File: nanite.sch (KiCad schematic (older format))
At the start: 13 parts

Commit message: Add values
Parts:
- C?: value C -> 100n
- D? (x2): value D_Zener -> 3.6V
- R?: value R -> 390
- R? (x2): value R -> 68
- R?: value R -> 1k5
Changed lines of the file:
@@
 P 3350 3100
 F 0 "D?" H 3350 3200 50  0000 C CNN
-F 1 "D_Zener" H 3350 3000 50  0000 C CNN
+F 1 "3.6V" H 3350 3000 50  0000 C CNN
 F 2 "" H 3350 3100 50  0000 C CNN
 F 3 "" H 3350 3100 50  0000 C CNN
@@
 P 3650 3350
 F 0 "D?" H 3650 3450 50  0000 C CNN
-F 1 "D_Zener" H 3650 3250 50  0000 C CNN
+F 1 "3.6V" H 3650 3250 50  0000 C CNN
 F 2 "" H 3650 3350 50  0000 C CNN
 F 3 "" H 3650 3350 50  0000 C CNN
@@
 P 6600 3800
 F 0 "R?" V 6680 3800 50  0000 C CNN
-F 1 "R" V 6600 3800 50  0000 C CNN
+F 1 "390" V 6600 3800 50  0000 C CNN
 F 2 "" V 6530 3800 50  0000 C CNN
 F 3 "" H 6600 3800 50  0000 C CNN
@@
 P 4450 2700
 F 0 "R?" V 4530 2700 50  0000 C CNN
-F 1 "R" V 4450 2700 50  0000 C CNN
+F 1 "68" V 4450 2700 50  0000 C CNN
 F 2 "" V 4380 2700 50  0000 C CNN
 F 3 "" H 4450 2700 50  0000 C CNN
@@
 P 3150 2150
 F 0 "R?" V 3230 2150 50  0000 C CNN
-F 1 "R" V 3150 2150 50  0000 C CNN
+F 1 "1k5" V 3150 2150 50  0000 C CNN
 F 2 "" V 3080 2150 50  0000 C CNN
 F 3 "" H 3150 2150 50  0000 C CNN
@@
 P 4050 2600
 F 0 "R?" V 4130 2600 50  0000 C CNN
-F 1 "R" V 4050 2600 50  0000 C CNN
+F 1 "68" V 4050 2600 50  0000 C CNN
 F 2 "" V 3980 2600 50  0000 C CNN
 F 3 "" H 4050 2600 50  0000 C CNN
@@
 P 6200 2300
 F 0 "C?" H 6225 2400 50  0000 L CNN
-F 1 "C" H 6225 2200 50  0000 L CNN
+F 1 "100n" H 6225 2200 50  0000 L CNN
 F 2 "" H 6238 2150 50  0000 C CNN
 F 3 "" H 6200 2300 50  0000 C CNN

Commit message: Annotate
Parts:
- gave numbers to parts that had none: 13
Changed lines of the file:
@@
 $EndDescr
 $Comp
-L ATtiny85 U?
+L ATtiny85 U1
 U 1 1 5A5BF0E7
 P 7050 2250
-F 0 "U?" H 7250 1800 60  0000 C CNN
+F 0 "U1" H 7250 1800 60  0000 C CNN
 F 1 "ATtiny85" H 7000 2500 60  0000 C CNN
 F 2 "" H 7050 2250 60  0001 C CNN
@@
 $EndComp
 $Comp
-L CONN_01X04 P?
+L CONN_01X04 P2
 U 1 1 5A5BF17D
 P 2650 4350
-F 0 "P?" H 2650 4600 50  0000 C CNN
+F 0 "P2" H 2650 4600 50  0000 C CNN
 F 1 "CONN_01X04" V 2750 4350 50  0000 C CNN
 F 2 "" H 2650 4350 50  0000 C CNN
@@
 $EndComp
 $Comp
-L CONN_01X04 P?
+L CONN_01X04 P3
 U 1 1 5A5BF1AA
 P 4200 4350
-F 0 "P?" H 4200 4600 50  0000 C CNN
+F 0 "P3" H 4200 4600 50  0000 C CNN
 F 1 "CONN_01X04" V 4300 4350 50  0000 C CNN
 F 2 "" H 4200 4350 50  0000 C CNN
@@
 $EndComp
 $Comp
-L D_Zener D?
+L D_Zener D1
 U 1 1 5A5BF22E
 P 3350 3100
-F 0 "D?" H 3350 3200 50  0000 C CNN
+F 0 "D1" H 3350 3200 50  0000 C CNN
 F 1 "3.6V" H 3350 3000 50  0000 C CNN
 F 2 "" H 3350 3100 50  0000 C CNN
@@
 $EndComp
 $Comp
-L D_Zener D?
+L D_Zener D2
 U 1 1 5A5BF26B
 P 3650 3350
-F 0 "D?" H 3650 3450 50  0000 C CNN
+F 0 "D2" H 3650 3450 50  0000 C CNN
 F 1 "3.6V" H 3650 3250 50  0000 C CNN
 F 2 "" H 3650 3350 50  0000 C CNN
@@
 $EndComp
 $Comp
-L R R?
+L R R4
 U 1 1 5A5BF29A
 P 6600 3800
-F 0 "R?" V 6680 3800 50  0000 C CNN
+F 0 "R4" V 6680 3800 50  0000 C CNN
 F 1 "390" V 6600 3800 50  0000 C CNN
 F 2 "" V 6530 3800 50  0000 C CNN
@@
 $EndComp
 $Comp
-L R R?
+L R R3
 U 1 1 5A5BF2D3
 P 4450 2700
-F 0 "R?" V 4530 2700 50  0000 C CNN
+F 0 "R3" V 4530 2700 50  0000 C CNN
 F 1 "68" V 4450 2700 50  0000 C CNN
 F 2 "" V 4380 2700 50  0000 C CNN
@@
 $EndComp
 $Comp
-L R R?
+L R R1
 U 1 1 5A5BF320
 P 3150 2150
-F 0 "R?" V 3230 2150 50  0000 C CNN
+F 0 "R1" V 3230 2150 50  0000 C CNN
 F 1 "1k5" V 3150 2150 50  0000 C CNN
 F 2 "" V 3080 2150 50  0000 C CNN
@@
 $EndComp
 $Comp
-L R R?
+L R R2
 U 1 1 5A5BF351
 P 4050 2600
-F 0 "R?" V 4130 2600 50  0000 C CNN
+F 0 "R2" V 4130 2600 50  0000 C CNN
 F 1 "68" V 4050 2600 50  0000 C CNN
 F 2 "" V 3980 2600 50  0000 C CNN
@@
 $EndComp
 $Comp
-L LED D?
+L LED D3
 U 1 1 5A5BF38B
 P 6600 4200
-F 0 "D?" H 6600 4300 50  0000 C CNN
+F 0 "D3" H 6600 4300 50  0000 C CNN
 F 1 "LED" H 6600 4100 50  0000 C CNN
 F 2 "" H 6600 4200 50  0000 C CNN
@@
 $EndComp
 $Comp
-L USB_OTG P?
+L USB_OTG P1
 U 1 1 5A5BF3BE
 P 2400 2600
-F 0 "P?" H 2725 2475 50  0000 C CNN
+F 0 "P1" H 2725 2475 50  0000 C CNN
 F 1 "USB_OTG" H 2400 2800 50  0000 C CNN
 F 2 "" V 2350 2500 50  0000 C CNN
@@
 $EndComp
 $Comp
-L C C?
+L C C1
 U 1 1 5A5BF438
 P 6200 2300
-F 0 "C?" H 6225 2400 50  0000 L CNN
+F 0 "C1" H 6225 2400 50  0000 L CNN
 F 1 "100n" H 6225 2200 50  0000 L CNN
 F 2 "" H 6238 2150 50  0000 C CNN
@@
 $EndComp
 $Comp
-L GND #PWR?
+L GND #PWR01
 U 1 1 5A5BF4AF
 P 6200 2650
-F 0 "#PWR?" H 6200 2400 50  0001 C CNN
+F 0 "#PWR01" H 6200 2400 50  0001 C CNN
 F 1 "GND" H 6200 2500 50  0000 C CNN
 F 2 "" H 6200 2650 50  0000 C CNN
@@
 $EndComp
 $Comp
-L VCC #PWR?
+L VCC #PWR02
 U 1 1 5A5C0227
 P 6200 1900
-F 0 "#PWR?" H 6200 1750 50  0001 C CNN
+F 0 "#PWR02" H 6200 1750 50  0001 C CNN
 F 1 "VCC" H 6200 2050 50  0000 C CNN
 F 2 "" H 6200 1900 50  0000 C CNN
@@
 $EndComp
 $Comp
-L VCC #PWR?
+L VCC #PWR03
 U 1 1 5A5C02C5
 P 6600 3550
-F 0 "#PWR?" H 6600 3400 50  0001 C CNN
+F 0 "#PWR03" H 6600 3400 50  0001 C CNN
 F 1 "VCC" H 6600 3700 50  0000 C CNN
 F 2 "" H 6600 3550 50  0000 C CNN
@@
 $EndComp
 $Comp
-L GND #PWR?
+L GND #PWR04
 U 1 1 5A5C04BD
 P 7750 4650
-F 0 "#PWR?" H 7750 4400 50  0001 C CNN
+F 0 "#PWR04" H 7750 4400 50  0001 C CNN
 F 1 "GND" H 7750 4500 50  0000 C CNN
 F 2 "" H 7750 4650 50  0000 C CNN
@@
 $EndComp
 $Comp
-L GND #PWR?
+L GND #PWR05
 U 1 1 5A5C08A1
 P 2850 3150
-F 0 "#PWR?" H 2850 2900 50  0001 C CNN
+F 0 "#PWR05" H 2850 2900 50  0001 C CNN
 F 1 "GND" H 2850 3000 50  0000 C CNN
 F 2 "" H 2850 3150 50  0000 C CNN
@@
 PB3
 $Comp
-L GND #PWR?
+L GND #PWR06
 U 1 1 5A5C23D2
 P 3350 3600
-F 0 "#PWR?" H 3350 3350 50  0001 C CNN
+F 0 "#PWR06" H 3350 3350 50  0001 C CNN
 F 1 "GND" H 3350 3450 50  0000 C CNN
 F 2 "" H 3350 3600 50  0000 C CNN
@@
 $EndComp
 $Comp
-L GND #PWR?
+L GND #PWR07
 U 1 1 5A5C2401
 P 3650 3600
-F 0 "#PWR?" H 3650 3350 50  0001 C CNN
+F 0 "#PWR07" H 3650 3350 50  0001 C CNN
 F 1 "GND" H 3650 3450 50  0000 C CNN
 F 2 "" H 3650 3600 50  0000 C CNN
@@
 Connection ~ 3150 2700
 $Comp
-L VCC #PWR?
+L VCC #PWR08
 U 1 1 5A5C2703
 P 3150 1600
-F 0 "#PWR?" H 3150 1450 50  0001 C CNN
+F 0 "#PWR08" H 3150 1450 50  0001 C CNN
 F 1 "VCC" H 3150 1750 50  0000 C CNN
 F 2 "" H 3150 1600 50  0000 C CNN
@@
 Connection ~ 3150 1800
 $Comp
-L SimpleSwitch U?
+L SimpleSwitch U2
 U 1 1 5A5C34F8
 P 7200 4650
-F 0 "U?" H 7350 4300 60  0000 C CNN
+F 0 "U2" H 7200 4550 60  0000 C CNN
 F 1 "Switch" H 7100 4800 39  0000 C CNN
 F 2 "" H 7200 4650 60  0001 C CNN

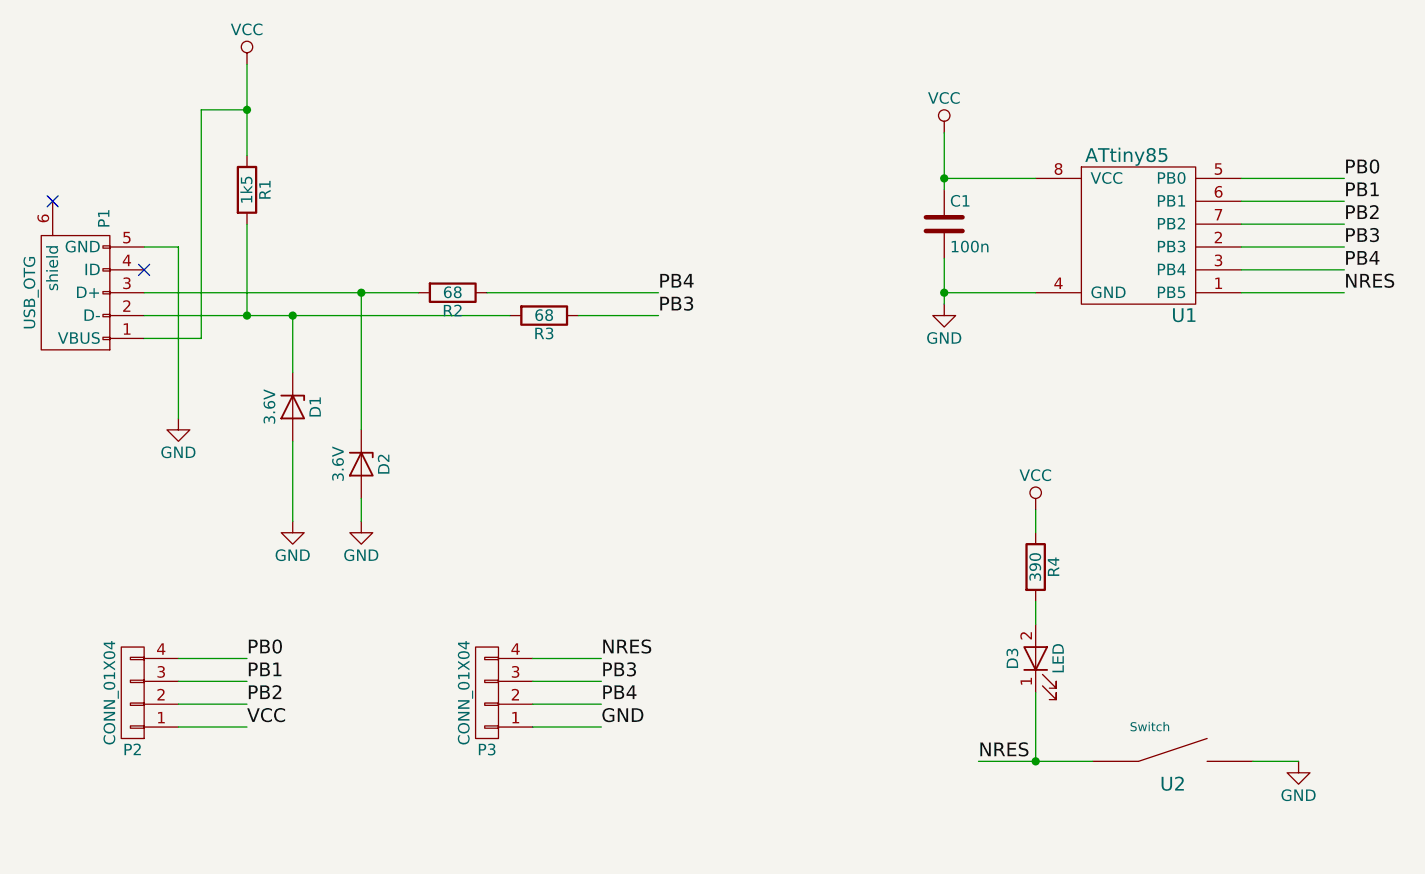
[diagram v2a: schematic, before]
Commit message: Change 100n to 22n
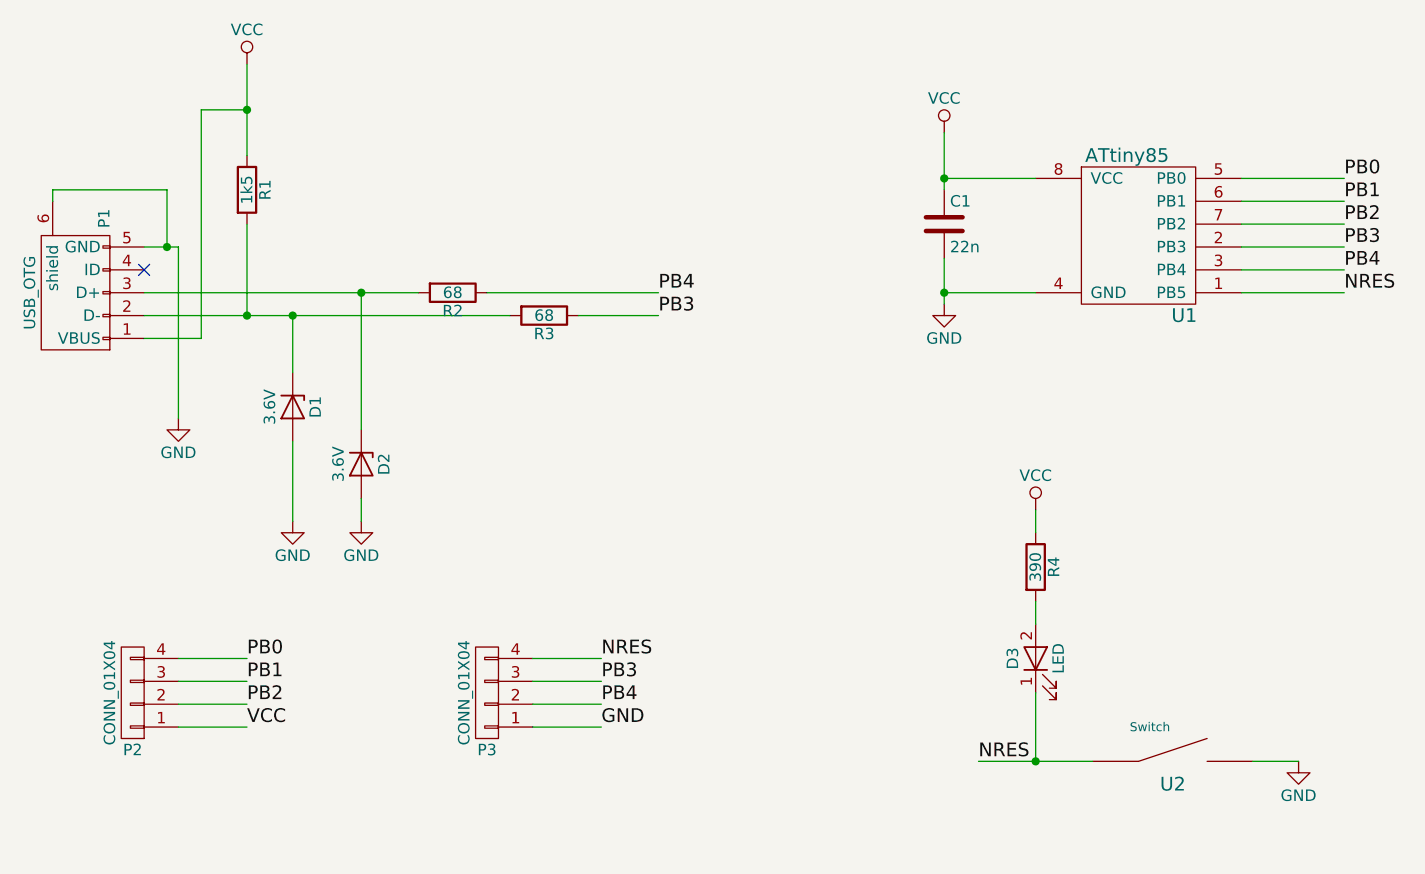
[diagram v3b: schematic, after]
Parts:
- C1: value 100n -> 22n
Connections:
- net GND: now also P1.6 (shield)
- no-connect marks 2 -> 1
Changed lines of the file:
@@
 P 6200 2300
 F 0 "C1" H 6225 2400 50  0000 L CNN
-F 1 "100n" H 6225 2200 50  0000 L CNN
+F 1 "22n" H 6225 2200 50  0000 L CNN
 F 2 "" H 6238 2150 50  0000 C CNN
 F 3 "" H 6200 2300 50  0000 C CNN
@@
 $EndComp
 NoConn ~ 2700 2500
-NoConn ~ 2300 2200
 Wire Wire Line
 	2700 2400 2850 2400
@@
 Wire Wire Line
 	7550 4650 7750 4650
+Wire Wire Line
+	2300 2200 2300 2150
+Wire Wire Line
+	2300 2150 2800 2150
+Wire Wire Line
+	2800 2150 2800 2400
+Connection ~ 2800 2400
 $EndSCHEMATC
